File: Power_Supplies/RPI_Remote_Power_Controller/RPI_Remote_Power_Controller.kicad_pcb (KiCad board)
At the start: 2 copper layers, 235 x 103.5 mm, 36 parts, among them J1 Screw_Terminal_01x02, J10 Screw_Terminal_01x03, J11 Raspberry_Pi_Zero_W, J12 Screw_Terminal_01x02, J2 Screw_Terminal_01x02, J3 Screw_Terminal_01x02, J4 Screw_Terminal_01x02, J5 Screw_Terminal_01x02, J6 Screw_Terminal_01x02, J7 Screw_Terminal_01x02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

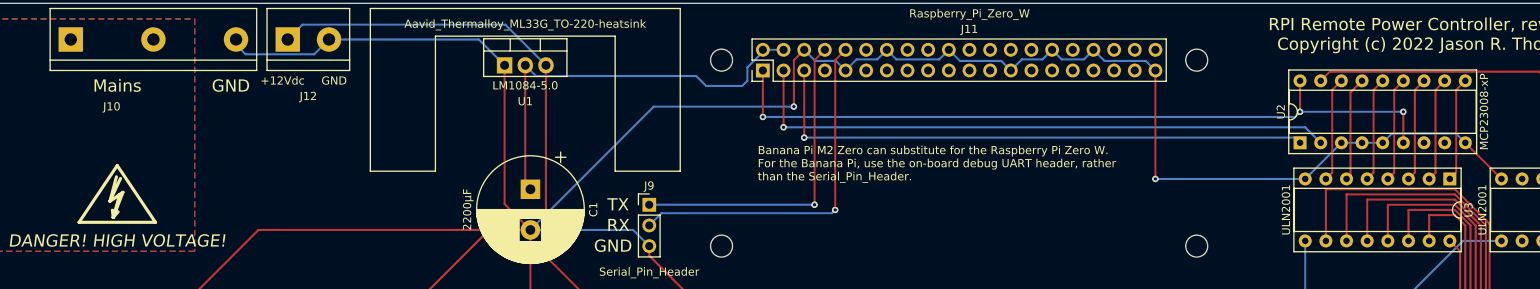
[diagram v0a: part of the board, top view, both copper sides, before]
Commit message: - We really are using ULN2003s. - Connect the ~RESET line of the MCP23008 to pin 40 of the GPIO   header.
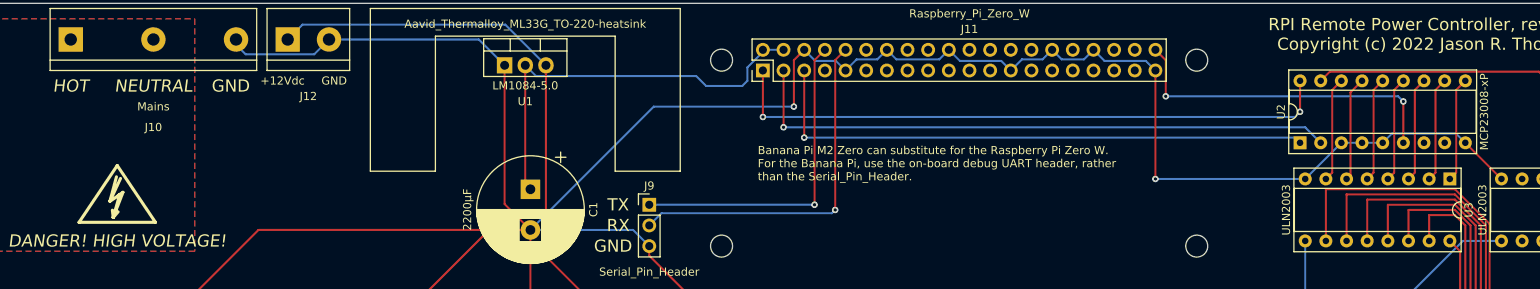
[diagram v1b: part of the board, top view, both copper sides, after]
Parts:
- U3, U4: value ULN2001 -> ULN2003
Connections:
- U2 pad 6: Net-(J11-Pad1) -> Net-(J11-Pad40)
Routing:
- net Net-(J11-Pad40): track 0.00 -> 40.8 mm, vias 0 -> 2
- net Net-(J11-Pad1): track 92.3 -> 75.8 mm, vias 3 -> 2
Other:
- board text added: "HOT"
- board text added: "NEUTRAL"
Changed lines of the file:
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@@
   (general
     (thickness 1.6)
-    (drawings 26)
-    (tracks 389)
+    (drawings 28)
+    (tracks 393)
     (zones 0)
     (modules 36)
@@
       (net 64 "Net-(U2-Pad14)"))
     (pad 6 thru_hole oval (at 0 12.7 90) (size 1.6 1.6) (drill 0.8) (layers *.Cu *.Mask)
-      (net 22 "Net-(J11-Pad1)"))
+      (net 50 "Net-(J11-Pad40)"))
     (pad 15 thru_hole oval (at 7.62 7.62 90) (size 1.6 1.6) (drill 0.8) (layers *.Cu *.Mask)
       (net 65 "Net-(U2-Pad15)"))
@@
       (effects (font (size 1 1) (thickness 0.15)))
     )
-    (fp_text value ULN2001 (at 3.81 20.11 90) (layer F.SilkS)
+    (fp_text value ULN2003 (at 3.81 20.11 90) (layer F.SilkS)
       (effects (font (size 1 1) (thickness 0.15)))
     )
@@
       (effects (font (size 1 1) (thickness 0.15)))
     )
-    (fp_text value ULN2001 (at 3.81 20.11 90) (layer F.SilkS)
+    (fp_text value ULN2003 (at 3.81 20.11 90) (layer F.SilkS)
       (effects (font (size 1 1) (thickness 0.15)))
     )
@@
     (descr "simple 3-pin terminal block, pitch 10.16mm, 600V")
     (tags "terminal block bornier3")
-    (fp_text reference J10 (at 5.05 8.255) (layer F.SilkS)
+    (fp_text reference J10 (at 10.16 10.795) (layer F.SilkS)
       (effects (font (size 1 1) (thickness 0.15)))
     )
@@
     )
   )
+  (gr_text NEUTRAL (at 123.825 113.03) (layer F.SilkS)
+    (effects (font (size 1.5 1.5) (thickness 0.3) italic))
+  )
+  (gr_text HOT (at 113.665 113.03) (layer F.SilkS)
+    (effects (font (size 1.5 1.5) (thickness 0.3) italic))
+  )
   (gr_text "Banana Pi M2 Zero can substitute for the Raspberry Pi Zero W.\nFor the Banana Pi, use the on-board debug UART header, rather\nthan the Serial_Pin_Header." (at 198.12 122.555) (layer F.SilkS)
     (effects (font (size 1 1) (thickness 0.15)) (justify left))
@@
     (effects (font (size 1.5 1.5) (thickness 0.3)))
   )
-  (gr_text Mains (at 119.38 113.03) (layer F.SilkS)
-    (effects (font (size 1.5 1.5) (thickness 0.3)))
+  (gr_text Mains (at 123.825 115.57) (layer F.SilkS)
+    (effects (font (size 1 1) (thickness 0.15)))
   )
   (gr_arc (start 316.865 106.68) (end 320.675 106.68) (angle -90) (layer Edge.Cuts) (width 0.05))
@@
   (via (at 264.795 116.205) (size 0.8) (drill 0.4) (layers F.Cu B.Cu) (net 22))
   (segment (start 264.795 112.395) (end 264.795 116.205) (width 0.25) (layer F.Cu) (net 22))
-  (via (at 277.495 116.205) (size 0.8) (drill 0.4) (layers F.Cu B.Cu) (net 22))
-  (segment (start 264.795 116.205) (end 277.495 116.205) (width 0.25) (layer B.Cu) (net 22))
-  (segment (start 277.495 116.205) (end 277.495 120.015) (width 0.25) (layer F.Cu) (net 22))
   (via (at 198.755 116.84) (size 0.8) (drill 0.4) (layers F.Cu B.Cu) (net 22))
   (segment (start 198.755 111.125) (end 198.755 116.84) (width 0.25) (layer F.Cu) (net 22))
@@
   (segment (start 264.16 119.38) (end 264.795 120.015) (width 0.25) (layer B.Cu) (net 25))
   (segment (start 203.835 119.38) (end 264.16 119.38) (width 0.25) (layer B.Cu) (net 25))
+  (via (at 248.285 114.3) (size 0.8) (drill 0.4) (layers F.Cu B.Cu) (net 50))
+  (segment (start 248.285 109.855) (end 248.285 114.3) (width 0.25) (layer F.Cu) (net 50))
+  (segment (start 247.015 108.585) (end 248.285 109.855) (width 0.25) (layer F.Cu) (net 50))
+  (via (at 277.495 114.935) (size 0.8) (drill 0.4) (layers F.Cu B.Cu) (net 50))
+  (segment (start 276.86 114.3) (end 277.495 114.935) (width 0.25) (layer B.Cu) (net 50))
+  (segment (start 248.285 114.3) (end 276.86 114.3) (width 0.25) (layer B.Cu) (net 50))
+  (segment (start 277.495 114.935) (end 277.495 120.015) (width 0.25) (layer F.Cu) (net 50))
   (segment (start 295.725953 164.125) (end 295.495 164.125) (width 0.25) (layer B.Cu) (net 51))
   (segment (start 142.160001 105.489999) (end 140.335 107.315) (width 0.25) (layer B.Cu) (net 51))

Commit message: Fits on 8.5 x 11.
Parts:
- moved J4 84.1 mm to (129.5, 121.3)
- moved J6 84.1 mm to (182.9, 121.3)
- moved REF** 84.1 mm to (254.6, 50.2)
- moved C1 84.1 mm to (108.0, 69.2)
- moved J1 84.1 mm to (49.5, 121.3)
- moved J10 84.1 mm to (51.4, 50.8)
- moved J12 84.1 mm to (78.1, 50.8)
- moved J2 84.1 mm to (76.2, 121.3)
- moved REF** 84.1 mm to (131.4, 53.3)
- moved REF** 84.1 mm to (254.6, 146.1)
- moved REF** 84.1 mm to (131.4, 76.2)
- moved SW6 84.1 mm to (187.3, 99.1)
- moved SW7 84.1 mm to (214.0, 99.1)
- moved U2 84.1 mm to (202.6, 63.5)
- moved J3 84.1 mm to (102.9, 121.3)
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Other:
- board size 235 x 103.5 mm -> 234.9 x 103.5 mm
